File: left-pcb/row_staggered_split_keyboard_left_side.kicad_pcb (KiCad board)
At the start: 2 copper layers, 165 x 132 mm, 177 parts, among them J1 Conn_01x02, SW1 SW_SPST, SW10 SW_SPST, SW11 SW_SPST, SW12 SW_SPST, SW13 SW_SPST, SW14 SW_SPST, SW15 SW_SPST, SW16 SW_SPST, SW17 SW_SPST, SW18 SW_SPST, SW19 SW_SPST, SW2 SW_SPST, SW20 SW_SPST, SW21 SW_SPST, SW22 SW_SPST, SW23 SW_SPST, SW24 SW_SPST, SW25 SW_SPST, SW26 SW_SPST, SW27 SW_SPST, SW28 SW_SPST, SW29 SW_SPST, SW3 SW_SPST, SW30 SW_SPST, SW31 SW_SPST, SW32 SW_SPST, SW33 SW_SPST, SW34 SW_SPST, SW35 SW_SPST, SW36 SW_SPST, SW37 SW_SPST, SW38 SW_SPST, SW39 SW_SPST, SW4 SW_SPST, SW40 SW_SPST, SW41 SW_SPST, SW5 SW_SPST, SW6 SW_SPST, SW7 SW_SPST, SW8 SW_SPST, SW9 SW_SPST, U1 SN74LVC1T45DBV

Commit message: applied feedback from coworker
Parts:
- moved C4 1.16 mm to (160.6, 44.5)
- moved C1 1.06 mm to (173.8, 45.0)
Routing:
- net GND: track 176.0 -> 178.2 mm
- net +5V: track 4.28 -> 5.44 mm
- net +3V3: track 4.96 -> 6.02 mm
- added copper zone on B.Cu, net GND

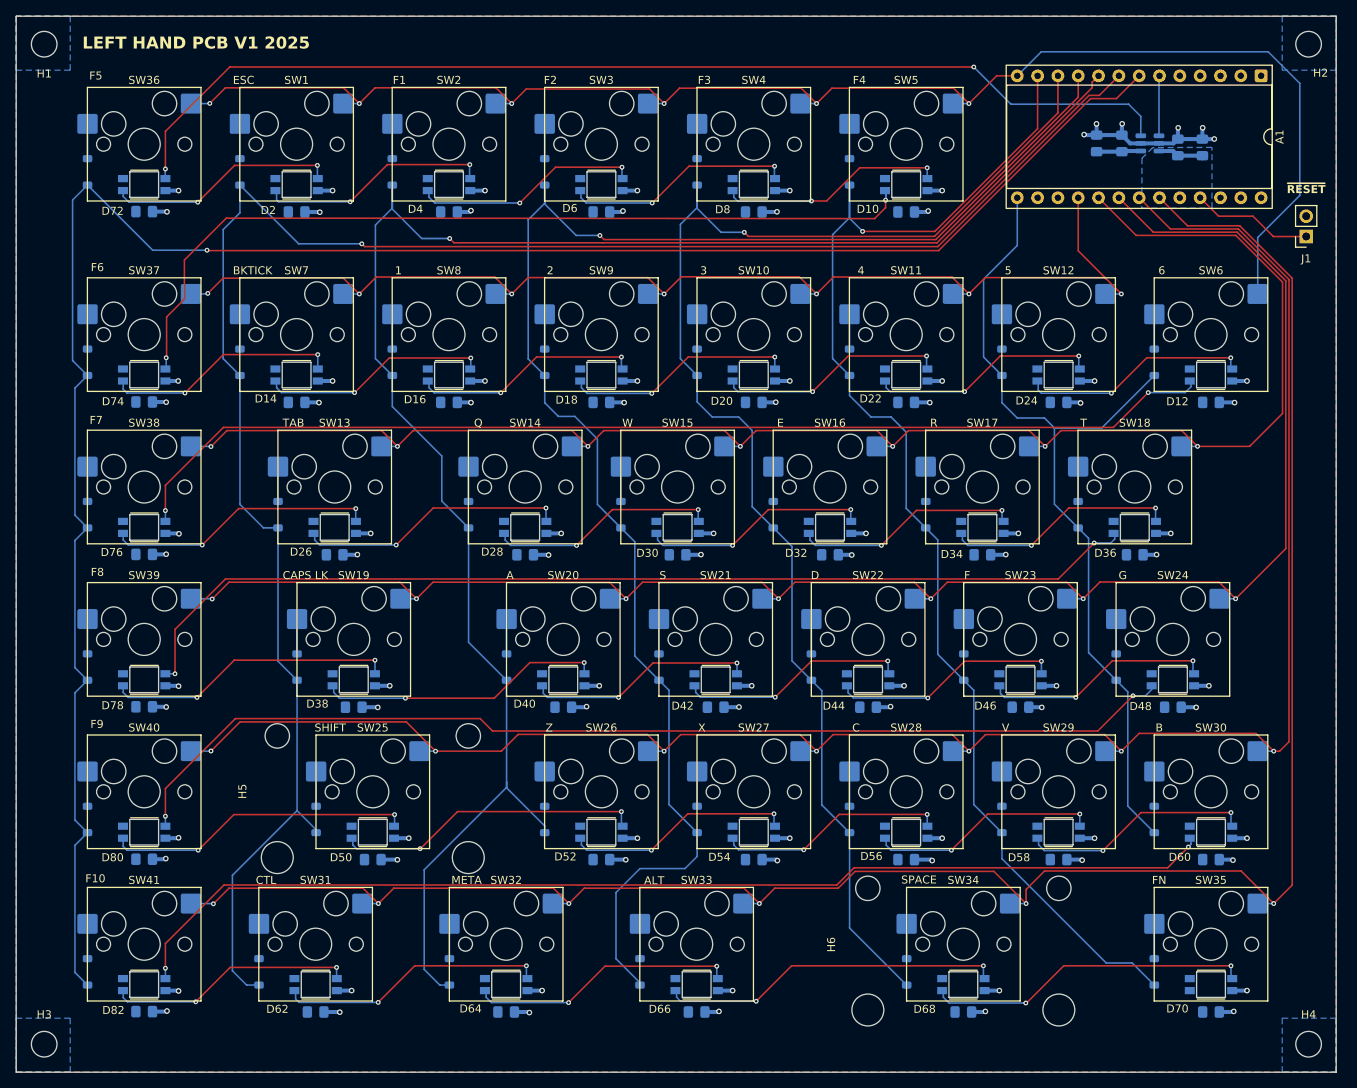
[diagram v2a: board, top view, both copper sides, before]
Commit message: adding mounting hole in center for additional support, and cleaning up tracks/zones
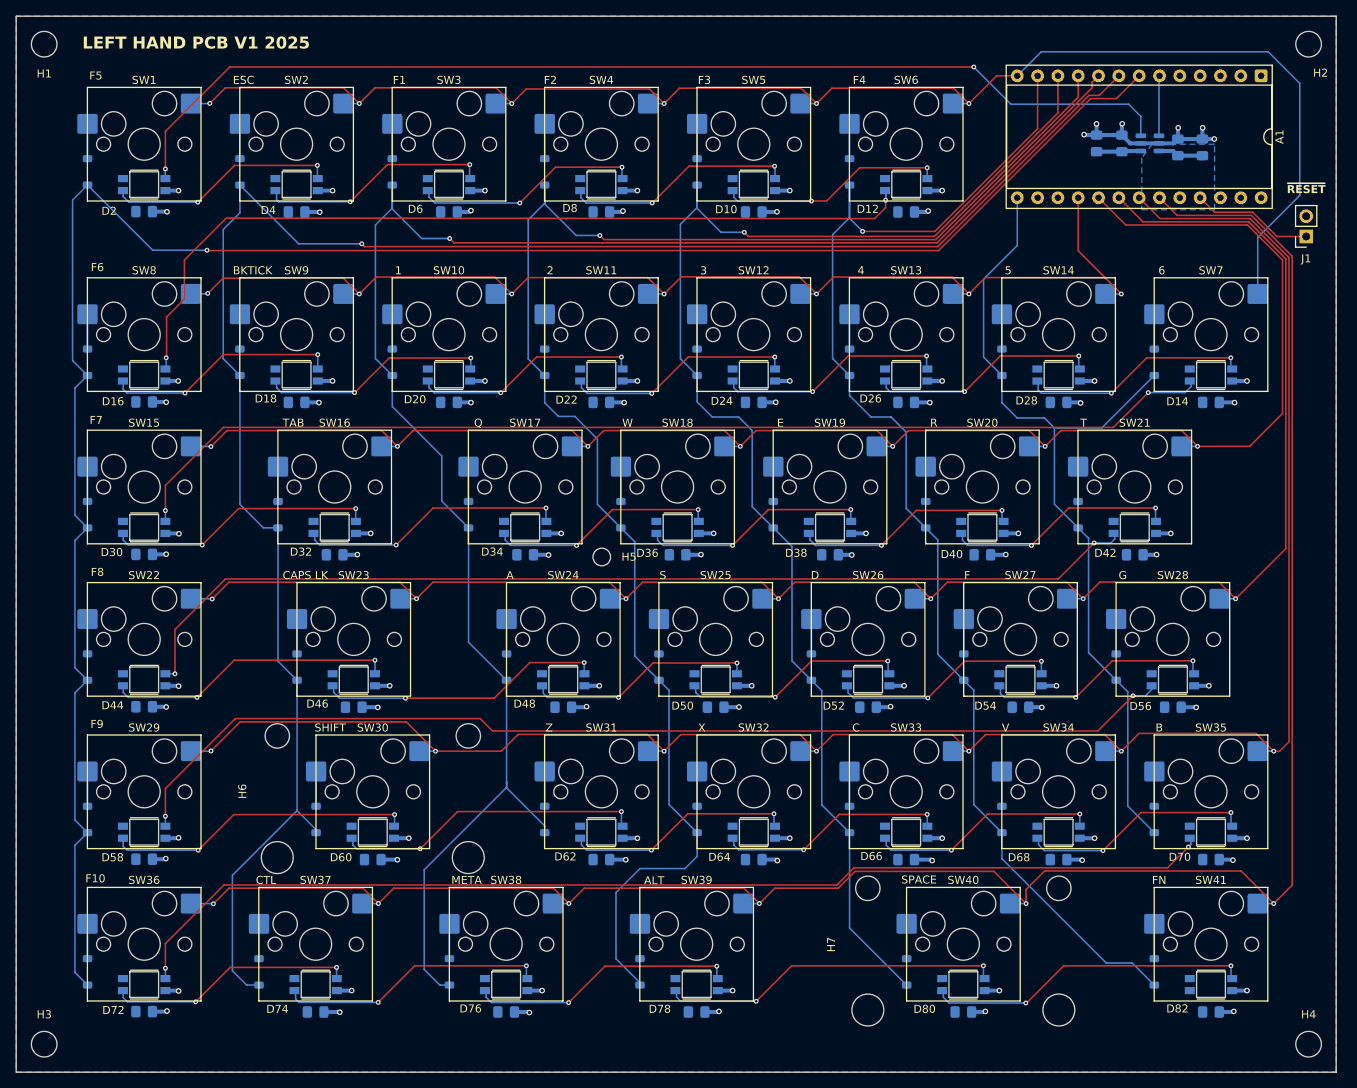
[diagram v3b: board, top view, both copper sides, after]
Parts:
- added H5: M2, MountingHole:MountingHole_2.2mm_M2, F.Cu at (98.7, 96.2)
- renumbered C9 to C10, C10 to C11, C41 to C12, C11 to C13, C12 to C14, C13 to C15, C14 to C16, C15 to C17, C16 to C18, C42 to C19, C17 to C20, C18 to C21, C19 to C22, C20 to C23, C21 to C24, C22 to C25, C43 to C26, C23 to C27, C24 to C28, C25 to C29, C26 to C30, C27 to C31, C28 to C32, C44 to C33, C29 to C34, C30 to C35, C31 to C36, C32 to C37, C33 to C38, C34 to C39, C45 to C40, C35 to C41, C36 to C42, C37 to C43, C38 to C44, C39 to C45, C40 to C5, C5 to C6, C6 to C7, C7 to C8, C8 to C9, D71 to D1, D8 to D10, D9 to D11, D10 to D12, D11 to D13, D12 to D14, D73 to D15, D74 to D16, D13 to D17, D14 to D18, D15 to D19, D72 to D2, D16 to D20, D17 to D21, D18 to D22, D19 to D23, D20 to D24, D21 to D25, D22 to D26, D23 to D27, D24 to D28, D75 to D29, D1 to D3, D76 to D30, D25 to D31, D26 to D32, D27 to D33, D28 to D34, D29 to D35, D30 to D36, D31 to D37, D32 to D38, D33 to D39, D2 to D4, D34 to D40, D35 to D41, D36 to D42, D77 to D43, D78 to D44, D37 to D45, D38 to D46, D39 to D47, D40 to D48, D41 to D49, D3 to D5, D42 to D50, D43 to D51, D44 to D52, D45 to D53, D46 to D54, D47 to D55, D48 to D56, D79 to D57, D80 to D58, D49 to D59, D4 to D6, D50 to D60, D51 to D61, D52 to D62, D53 to D63, D54 to D64, D55 to D65, D56 to D66, D57 to D67, D58 to D68, D59 to D69, D5 to D7, D60 to D70, D81 to D71, D82 to D72, D61 to D73, D62 to D74, D63 to D75, D64 to D76, D65 to D77, D66 to D78, D67 to D79, D6 to D8, D68 to D80, D69 to D81, D70 to D82, D7 to D9, H5 to H6, H6 to H7, SW36 to SW1, SW8 to SW10, SW9 to SW11, SW10 to SW12, SW11 to SW13, SW12 to SW14, SW38 to SW15, SW13 to SW16, SW14 to SW17, SW15 to SW18, SW16 to SW19, SW1 to SW2, SW17 to SW20, SW18 to SW21, SW39 to SW22, SW19 to SW23, SW20 to SW24, SW21 to SW25, SW22 to SW26, SW23 to SW27, SW24 to SW28, SW40 to SW29, SW2 to SW3, SW25 to SW30, SW26 to SW31, SW27 to SW32, SW28 to SW33, SW29 to SW34, SW30 to SW35, SW41 to SW36, SW31 to SW37, SW32 to SW38, SW33 to SW39, SW3 to SW4, SW34 to SW40, SW35 to SW41, SW4 to SW5, SW5 to SW6, SW6 to SW7, SW37 to SW8, SW7 to SW9
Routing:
- net /ROW5: track 242.2 -> 243.8 mm
- net /ROW3: track 203.8 -> 205.4 mm
- net /ROW4: track 220.4 -> 222.0 mm
- net /ROW6: track 257.8 -> 259.4 mm
- removed copper zone on B.Cu, net GND
